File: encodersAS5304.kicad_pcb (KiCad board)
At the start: 2 copper layers, 11 parts, among them P1 CONN_01X02, P101 CONN_01X02, P102 CONN_01X02, P2 CONN_01X02, P3 CONN_01X02, P4 CONN_01X02, P5 CONN_01X02, P6 CONN_01X02, U101 AS5304

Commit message: placa con forma apropiada y dimensiones exactas. Falta enrutado
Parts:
- removed P1, P2, P3, P4, P5, P6: CONN_01X02, Pin_Headers:Pin_Header_Straight_1x02
- added P103: Pow, Pin_Headers:Pin_Header_Straight_1x02, F.Cu at (163.6, 119.6)
- added P104: Pow, Pin_Headers:Pin_Header_Straight_1x02, F.Cu at (163.6, 102.6)
- added P105: C1, Pin_Headers:Pin_Header_Straight_1x02, F.Cu at (141.8, 116.2)
- added P106: C1, Pin_Headers:Pin_Header_Straight_1x02, F.Cu at (141.8, 119.6)
- added P107: C1, Pin_Headers:Pin_Header_Straight_1x02, F.Cu at (141.8, 112.8)
- added P108: Pow, Pin_Headers:Pin_Header_Straight_1x02, F.Cu at (163.6, 109.4)
- added P109: Pow, Pin_Headers:Pin_Header_Straight_1x02, F.Cu at (163.6, 106.0)
- added P110: Pow, Pin_Headers:Pin_Header_Straight_1x02, F.Cu at (163.6, 116.2)
- added P111: C1, Pin_Headers:Pin_Header_Straight_1x02, F.Cu at (141.8, 106.0)
- added P112: C1, Pin_Headers:Pin_Header_Straight_1x02, F.Cu at (141.8, 102.6)
- P101: value CONN_01X02 -> C1
- P102: value CONN_01X02 -> Pow
- moved C101 19.7 mm to (142.4, 97.0), turned to 270 degrees
- moved C102 5.26 mm to (160.8, 97.0), turned to 270 degrees
- moved P102 4.60 mm to (163.6, 112.8)
- moved P101 2.52 mm to (141.8, 109.4)
- moved U101 1.61 mm to (151.8, 94.5)
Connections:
- U101 pad 10: Net-(U101-Pad10) -> (no net)
- U101 pad 11: Net-(U101-Pad11) -> (no net)
- U101 pad 12: Net-(U101-Pad12) -> (no net)
- U101 pad 13: Net-(U101-Pad13) -> (no net)
- U101 pad 14: Net-(U101-Pad14) -> (no net)
- U101 pad 17: Net-(U101-Pad17) -> (no net)
- U101 pad 18: Net-(U101-Pad18) -> (no net)
- U101 pad 19: Net-(U101-Pad19) -> (no net)
- U101 pad 5: Net-(U101-Pad5) -> (no net)
- U101 pad 6: Net-(U101-Pad6) -> (no net)
- U101 pad 8: Net-(U101-Pad8) -> (no net)
- U101 pad 9: Net-(U101-Pad9) -> (no net)
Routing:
- net GND: track 63.1 -> 0.00 mm, vias 2 -> 0
- net VDD: track 48.1 -> 0.00 mm, vias 1 -> 0
- net A: track 28.2 -> 0.00 mm
- net B: track 26.4 -> 0.00 mm
- net (no net): track 0.00 -> 1.00 mm
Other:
- board outline added: 28 x 31 mm

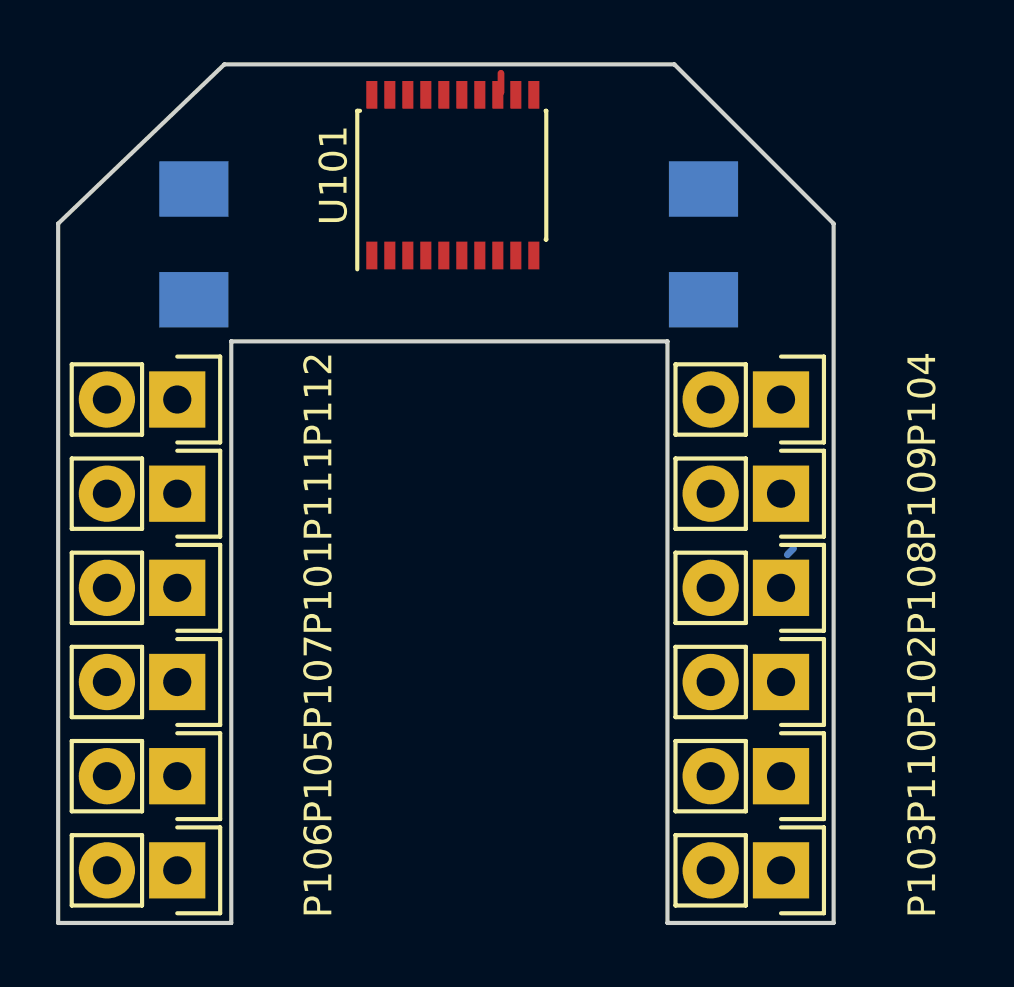
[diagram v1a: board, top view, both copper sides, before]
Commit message: enrutada + plano de masa en las dos capas
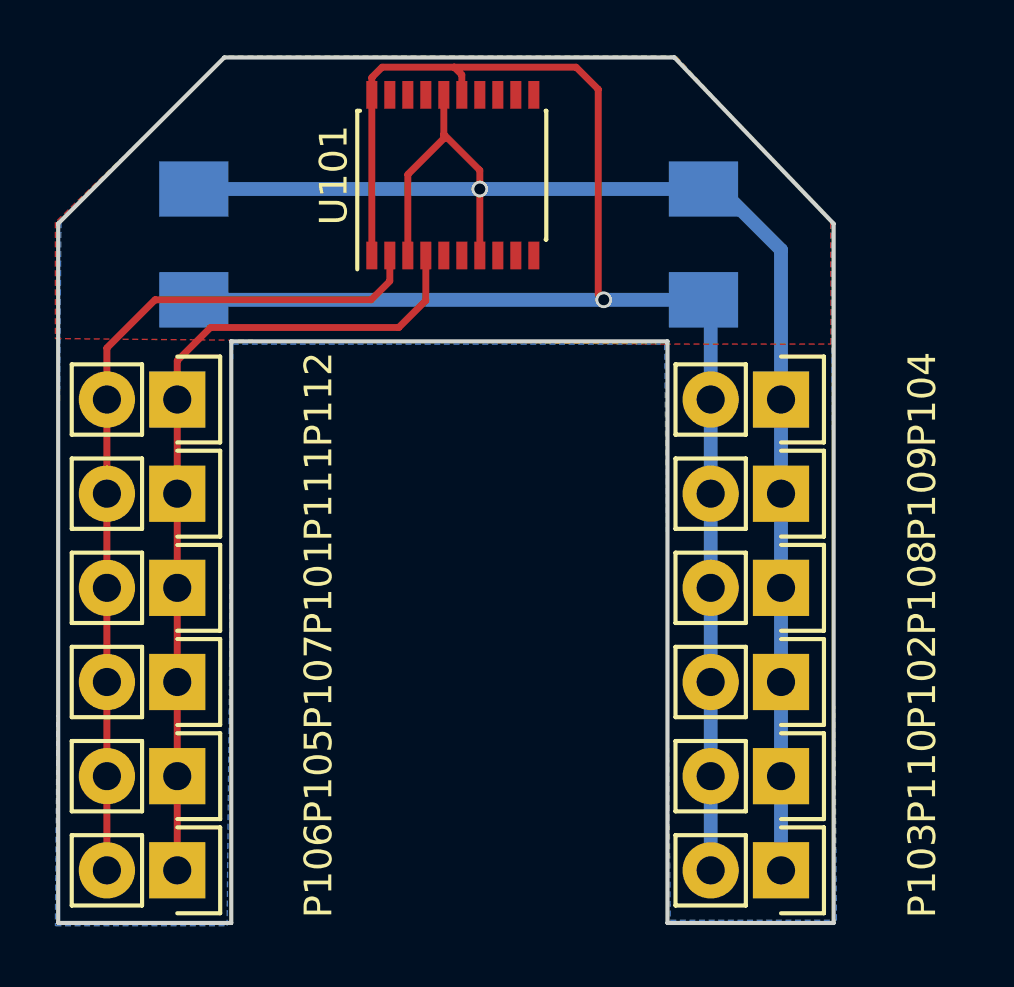
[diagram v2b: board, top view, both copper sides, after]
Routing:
- net GND: track 0.00 -> 66.6 mm, vias 0 -> 1
- net VDD: track 0.00 -> 63.8 mm, vias 0 -> 1
- net A: track 0.00 -> 31.0 mm
- net B: track 0.00 -> 29.9 mm
- net (no net): track 1.00 -> 0.00 mm
- added copper zone on B.Cu, net GND
- added copper zone on F.Cu, net GND
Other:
- board size 28 x 31 mm -> 28 x 31.2 mm
- net class power added: clearance 0.25, trace_width 0.5, via_dia 0.6, via_drill 0.4
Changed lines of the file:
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@@
   (general
     (links 32)
-    (no_connects 32)
-    (area 137.424999 90.424999 165.575001 121.575001)
+    (no_connects 0)
+    (area 137.224999 90.174999 169.725 121.853571)
     (thickness 1.6)
     (drawings 10)
-    (tracks 2)
+    (tracks 59)
     (zones 0)
     (modules 15)
@@
     (add_net VDD)
   )
+  (net_class power ""
+    (clearance 0.25)
+    (trace_width 0.5)
+    (via_dia 0.6)
+    (via_drill 0.4)
+    (uvia_dia 0.3)
+    (uvia_drill 0.1)
+  )
   (module Capacitors_SMD:C_1210_HandSoldering (layer B.Cu)
     (at 142.4 97 270)
@@
     )
   )
-  (gr_line (start 159.75 90.5) (end 143.5 90.5) (angle 90) (layer Edge.Cuts) (width 0.15))
-  (gr_line (start 165.5 96.25) (end 159.75 90.5) (angle 90) (layer Edge.Cuts) (width 0.15))
+  (gr_line (start 159.75 90.25) (end 143.5 90.25) (angle 90) (layer Edge.Cuts) (width 0.15))
+  (gr_line (start 165.5 96.25) (end 159.75 90.25) (angle 90) (layer Edge.Cuts) (width 0.15))
   (gr_line (start 165.5 121.5) (end 165.5 96.25) (angle 90) (layer Edge.Cuts) (width 0.15))
   (gr_line (start 159.5 121.5) (end 165.5 121.5) (angle 90) (layer Edge.Cuts) (width 0.15))
-  (gr_line (start 137.5 96.25) (end 143.5 90.5) (angle 90) (layer Edge.Cuts) (width 0.15))
+  (gr_line (start 137.5 96.25) (end 143.5 90.25) (angle 90) (layer Edge.Cuts) (width 0.15))
   (gr_line (start 137.5 121.5) (end 137.5 96.25) (angle 90) (layer Edge.Cuts) (width 0.15))
   (gr_line (start 143.75 121.5) (end 137.5 121.5) (angle 90) (layer Edge.Cuts) (width 0.15))
@@
   (gr_line (start 143.75 121.5) (end 143.75 100.5) (angle 90) (layer Edge.Cuts) (width 0.15))
   (gr_line (start 159.5 121.5) (end 159.5 100.5) (angle 90) (layer Edge.Cuts) (width 0.15))
-  (segment (start 153.487 91.511) (end 153.487 90.826) (width 0.25) (layer F.Cu) (net 0))
-  (segment (start 163.83 108.204) (end 164.052 107.982) (width 0.25) (layer B.Cu) (net 0))
+  (via (at 152.725 95) (size 0.6) (drill 0.4) (layers F.Cu B.Cu) (net 1))
+  (segment (start 160.8 95) (end 152.8 95) (width 0.25) (layer B.Cu) (net 1))
+  (segment (start 152.8 95) (end 152.725 95) (width 0.25) (layer B.Cu) (net 1))
+  (segment (start 152.725 97.4) (end 152.725 95) (width 0.25) (layer F.Cu) (net 1))
+  (segment (start 152.725 95) (end 152.725 94.325) (width 0.25) (layer F.Cu) (net 1))
+  (segment (start 152.725 94.325) (end 151.425 93.025) (width 0.25) (layer F.Cu) (net 1))
+  (segment (start 150.125 97.4) (end 150.125 94.475) (width 0.25) (layer F.Cu) (net 1))
+  (segment (start 151.425 93.175) (end 151.425 93.025) (width 0.25) (layer F.Cu) (net 1))
+  (segment (start 151.425 93.025) (end 151.425 91.6) (width 0.25) (layer F.Cu) (net 1))
+  (segment (start 150.125 94.475) (end 151.425 93.175) (width 0.25) (layer F.Cu) (net 1))
+  (segment (start 160.8 95) (end 142.4 95) (width 0.5) (layer B.Cu) (net 1))
+  (segment (start 163.6 119.6) (end 163.6 116.2) (width 0.5) (layer B.Cu) (net 1))
+  (segment (start 163.6 116.2) (end 163.6 112.8) (width 0.5) (layer B.Cu) (net 1))
+  (segment (start 163.6 112.8) (end 163.6 109.4) (width 0.5) (layer B.Cu) (net 1))
+  (segment (start 163.6 109.4) (end 163.6 106) (width 0.5) (layer B.Cu) (net 1))
+  (segment (start 163.6 106) (end 163.6 102.6) (width 0.5) (layer B.Cu) (net 1))
+  (segment (start 163.6 102.6) (end 163.6 97.2) (width 0.5) (layer B.Cu) (net 1))
+  (segment (start 163.6 97.2) (end 161.4 95) (width 0.5) (layer B.Cu) (net 1))
+  (segment (start 161.4 95) (end 160.8 95) (width 0.5) (layer B.Cu) (net 1))
+  (segment (start 151.8 90.6) (end 156.2 90.6) (width 0.25) (layer F.Cu) (net 2))
+  (segment (start 157.2 99) (end 160.8 99) (width 0.25) (layer B.Cu) (net 2))
+  (via (at 157.2 99) (size 0.6) (drill 0.4) (layers F.Cu B.Cu) (net 2))
+  (segment (start 157 98.8) (end 157.2 99) (width 0.25) (layer F.Cu) (net 2))
+  (segment (start 157 91.4) (end 157 98.8) (width 0.25) (layer F.Cu) (net 2))
+  (segment (start 156.2 90.6) (end 157 91.4) (width 0.25) (layer F.Cu) (net 2))
+  (segment (start 148.825 91.6) (end 148.825 90.975) (width 0.25) (layer F.Cu) (net 2))
+  (segment (start 152.075 90.875) (end 152.075 91.6) (width 0.25) (layer F.Cu) (net 2))
+  (segment (start 151.8 90.6) (end 152.075 90.875) (width 0.25) (layer F.Cu) (net 2))
+  (segment (start 149.2 90.6) (end 151.8 90.6) (width 0.25) (layer F.Cu) (net 2))
+  (segment (start 148.825 90.975) (end 149.2 90.6) (width 0.25) (layer F.Cu) (net 2))
+  (segment (start 148.825 97.4) (end 148.825 91.6) (width 0.25) (layer F.Cu) (net 2))
+  (segment (start 160.8 99) (end 142.4 99) (width 0.5) (layer B.Cu) (net 2))
+  (segment (start 161.06 102.6) (end 161.06 106) (width 0.5) (layer B.Cu) (net 2))
+  (segment (start 161.06 106) (end 161.06 109.4) (width 0.5) (layer B.Cu) (net 2))
+  (segment (start 161.06 109.4) (end 161.06 112.8) (width 0.5) (layer B.Cu) (net 2))
+  (segment (start 161.06 112.8) (end 161.06 116.2) (width 0.5) (layer B.Cu) (net 2))
+  (segment (start 161.06 116.2) (end 161.06 119.6) (width 0.5) (layer B.Cu) (net 2))
+  (segment (start 161.06 102.6) (end 161.06 99.26) (width 0.5) (layer B.Cu) (net 2))
+  (segment (start 161.06 99.26) (end 160.8 99) (width 0.5) (layer B.Cu) (net 2))
+  (segment (start 141.8 102.6) (end 141.8 106) (width 0.25) (layer F.Cu) (net 3))
+  (segment (start 141.8 106) (end 141.8 109.4) (width 0.25) (layer F.Cu) (net 3))
+  (segment (start 141.8 109.4) (end 141.8 112.8) (width 0.25) (layer F.Cu) (net 3))
+  (segment (start 141.8 112.8) (end 141.8 116.2) (width 0.25) (layer F.Cu) (net 3))
+  (segment (start 141.8 116.2) (end 141.8 119.6) (width 0.25) (layer F.Cu) (net 3))
+  (segment (start 150.775 97.4) (end 150.775 99.025) (width 0.25) (layer F.Cu) (net 3))
+  (segment (start 141.8 101.2) (end 141.8 102.6) (width 0.25) (layer F.Cu) (net 3))
+  (segment (start 143 100) (end 141.8 101.2) (width 0.25) (layer F.Cu) (net 3))
+  (segment (start 149.8 100) (end 143 100) (width 0.25) (layer F.Cu) (net 3))
+  (segment (start 150.775 99.025) (end 149.8 100) (width 0.25) (layer F.Cu) (net 3))
+  (segment (start 139.26 119.6) (end 139.26 116.2) (width 0.25) (layer F.Cu) (net 4))
+  (segment (start 139.26 116.2) (end 139.26 112.8) (width 0.25) (layer F.Cu) (net 4))
+  (segment (start 139.26 112.8) (end 139.26 109.4) (width 0.25) (layer F.Cu) (net 4))
+  (segment (start 139.26 109.4) (end 139.26 106) (width 0.25) (layer F.Cu) (net 4))
+  (segment (start 139.26 106) (end 139.26 102.6) (width 0.25) (layer F.Cu) (net 4))
+  (segment (start 149.475 97.4) (end 149.475 98.325) (width 0.25) (layer F.Cu) (net 4))
+  (segment (start 139.26 100.74) (end 139.26 102.6) (width 0.25) (layer F.Cu) (net 4))
+  (segment (start 141 99) (end 139.26 100.74) (width 0.25) (layer F.Cu) (net 4))
+  (segment (start 148.8 99) (end 141 99) (width 0.25) (layer F.Cu) (net 4))
+  (segment (start 149.475 98.325) (end 148.8 99) (width 0.25) (layer F.Cu) (net 4))
+  (zone (net 2) (net_name GND) (layer B.Cu) (hatch edge 0.508)
+    (connect_pads (clearance 0.508))
+    (min_thickness 0.254)
+    (fill (arc_segments 16) (thermal_gap 0.508) (thermal_bridge_width 0.508))
+    (polygon
+      (pts
+        (xy 159.4 100.6) (xy 159.6 121.4) (xy 165.6 121.4) (xy 165.4 96.2) (xy 159.8 90.2)
+        (xy 143.6 90.2) (xy 137.6 96.2) (xy 137.4 121.6) (xy 143.6 121.6) (xy 143.8 100.6)
+      )
+    )
+  )
+  (zone (net 2) (net_name GND) (layer F.Cu) (hatch edge 0.508)
+    (connect_pads (clearance 0.508))
+    (min_thickness 0.254)
+    (fill (arc_segments 16) (thermal_gap 0.508) (thermal_bridge_width 0.508))
+    (polygon
+      (pts
+        (xy 159.4 100.6) (xy 165.4 100.6) (xy 165.4 96.2) (xy 159.8 90.2) (xy 143.6 90.2)
+        (xy 137.4 96.2) (xy 137.4 100.4)
+      )
+    )
+  )
 )
